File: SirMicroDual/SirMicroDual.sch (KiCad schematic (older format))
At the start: 38 parts, among them J1 Conn_01x16, J2 Conn_01x16, J3 USB_B_Micro, Q1 Q_DUAL_PMOS_S1G1D2S2G2D1, U1 ATmega32U4-MU, U2 AP2127K-3.3, U3 AP1117-50, Y1 Resonator

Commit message: Layout updated and silkscreen revised
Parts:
- removed C11: 22uF, Capacitor_Tantalum_SMD:CP_EIA-3216-18_Kemet-A_Pad1.58x1.35mm_HandSolder, symbol Device:CP
- added C?: 22uF, Capacitor_Tantalum_SMD:CP_EIA-3216-18_Kemet-A_Pad1.58x1.35mm_HandSolder, symbol Device:CP
- U2: value AP2127K-3.3 -> AP2112K-3.3
- Y1: value Resonator -> 16MHz
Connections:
- net GND: now also C?.2
- net at C2.1, Q1.1 (S), U3.3 (VI): now also C?.1
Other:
- moved on the sheet: C10, C2, C9, JP1, JP2, Q1A, R6, U2

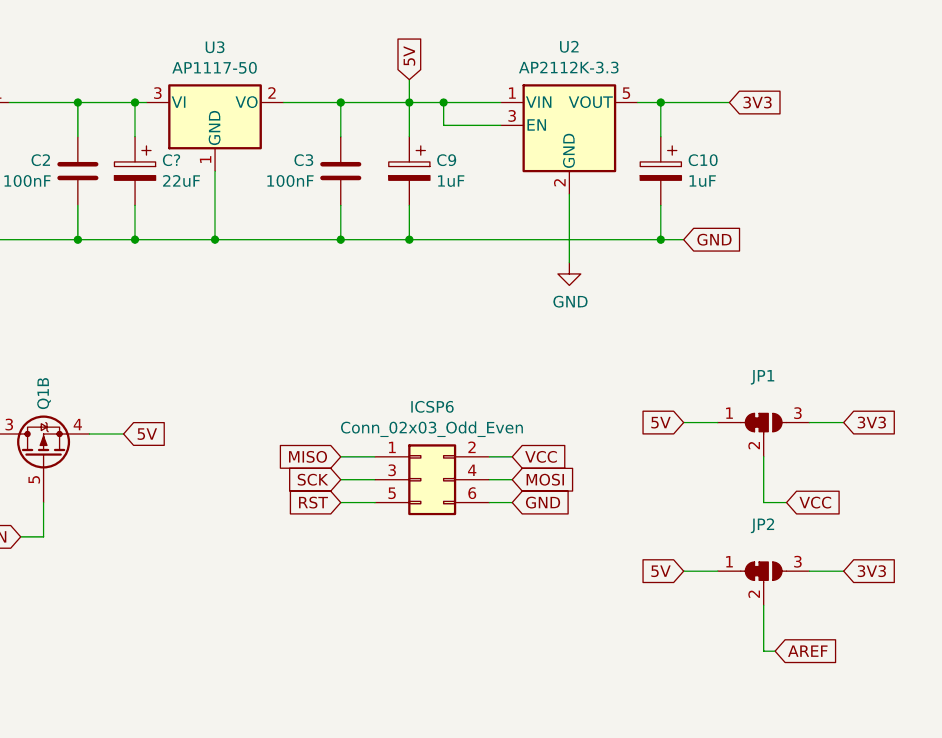
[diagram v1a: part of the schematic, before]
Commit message: LDO changed
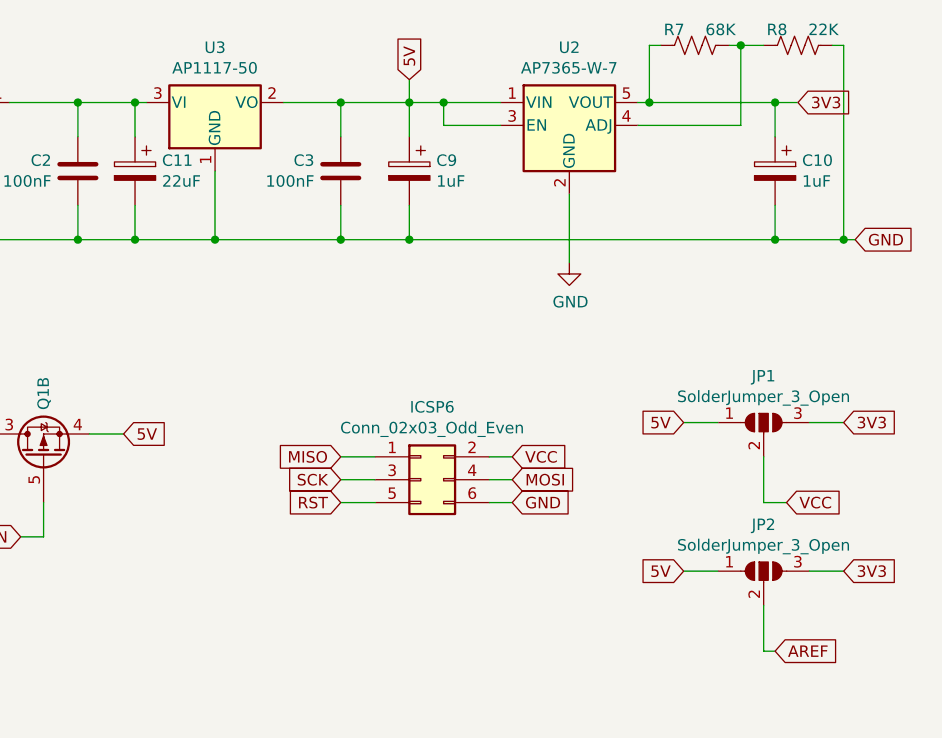
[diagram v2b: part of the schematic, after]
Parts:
- removed JP1, JP2: SolderJumper_3_Bridged12, Jumper:SolderJumper-3_P1.3mm_Bridged12_RoundedPad1.0x1.5mm, symbol Jumper:SolderJumper_3_Bridged12
- removed U2: AP2112K-3.3, Package_TO_SOT_SMD:SOT-23-5, symbol Regulator_Linear:AP2127K-3.3
- added JP1, JP2: SolderJumper_3_Open, Jumper:SolderJumper-3_P1.3mm_Open_RoundedPad1.0x1.5mm, symbol Jumper:SolderJumper_3_Open
- added R7: 68K, Resistor_SMD:R_0603_1608Metric, symbol Device:R_US
- added R8: 22K, Resistor_SMD:R_0603_1608Metric, symbol Device:R_US
- added U2: AP7365-W-7, Package_TO_SOT_SMD:SOT-23-5, symbol Regulator_Linear:AP2127K-ADJ
- F1: footprint Resistor_SMD:R_1210_3225Metric_Pad1.42x2.65mm_HandSolder -> Resistor_SMD:R_1206_3216Metric
- gave numbers to parts that had none: 1
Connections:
- net 3V3: now also JP1.3 (B), JP2.3 (B), R7.1, U2.5 (VOUT)
- net 5V: now also JP1.1 (A), JP2.1 (A), U2.1 (VIN), U2.3 (EN)
- net AREF: now also JP2.2 (C)
- net GND: now also R8.2, U2.2 (GND)
- net VCC: now also JP1.2 (C)
- new net: R7.2, R8.1, U2.4 (ADJ)
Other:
- moved on the sheet: C10
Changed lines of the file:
@@
 F 0 "F1" H 2088 2796 50  0000 L CNN
 F 1 "500mA" H 2088 2705 50  0000 L CNN
-F 2 "Resistor_SMD:R_1210_3225Metric_Pad1.42x2.65mm_HandSolder" H 2050 2550 50  0001 L CNN
+F 2 "Resistor_SMD:R_1206_3216Metric" H 2050 2550 50  0001 L CNN
 F 3 "~" H 2000 2750 50  0001 C CNN
 	1    2000 2750
@@
 L Device:CP C10
 U 1 1 5D5B70AC
-P 9900 1850
-F 0 "C10" H 9782 1896 50  0000 R CNN
-F 1 "1uF" H 9782 1805 50  0000 R CNN
-F 2 "Capacitor_SMD:C_0805_2012Metric_Pad1.15x1.40mm_HandSolder" H 9938 1700 50  0001 C CNN
-F 3 "~" H 9900 1850 50  0001 C CNN
-	1    9900 1850
+P 10400 1850
+F 0 "C10" H 10282 1896 50  0000 R CNN
+F 1 "1uF" H 10282 1805 50  0000 R CNN
+F 2 "Capacitor_SMD:C_0805_2012Metric_Pad1.15x1.40mm_HandSolder" H 10438 1700 50  0001 C CNN
+F 3 "~" H 10400 1850 50  0001 C CNN
+	1    10400 1850
 	-1   0    0    -1
 $EndComp
 Wire Wire Line
-	9900 1700 9900 1550
+	10400 1700 10400 1550
 $Comp
 L Device:CP C9
@@
 Text GLabel 2000 2350 0    50   Input ~ 0
 VUSB
-Text GLabel 10200 1550 2    50   Input ~ 0
+Text GLabel 10500 1550 2    50   Input ~ 0
 3V3
 Text GLabel 5150 4850 2    50   Input ~ 0
@@
 5V
 Wire Wire Line
-	10200 1550 9900 1550
-Connection ~ 9900 1550
+	10500 1550 10400 1550
+Connection ~ 10400 1550
 Text GLabel 9400 4800 0    50   Input ~ 0
 3V3
@@
 Text GLabel 2400 1450 0    50   Input ~ 0
 VCC
-$Comp
-L Jumper:SolderJumper_3_Bridged12 JP1
-U 1 1 5D43EA60
-P 10350 2950
-F 0 "JP1" H 10350 3153 50  0000 C CNN
-F 1 "SolderJumper_3_Bridged12" H 10350 3063 50  0001 C CNN
-F 2 "Jumper:SolderJumper-3_P1.3mm_Bridged12_RoundedPad1.0x1.5mm" H 10350 2950 50  0001 C CNN
-F 3 "~" H 10350 2950 50  0001 C CNN
-	1    10350 2950
-	1    0    0    -1
-$EndComp
 Text GLabel 10000 2950 0    50   Input ~ 0
 5V
@@
 Wire Wire Line
 	10150 2950 10000 2950
-$Comp
-L Jumper:SolderJumper_3_Bridged12 JP2
-U 1 1 5D523778
-P 10350 3600
-F 0 "JP2" H 10350 3803 50  0000 C CNN
-F 1 "SolderJumper_3_Bridged12" H 10350 3713 50  0001 C CNN
-F 2 "Jumper:SolderJumper-3_P1.3mm_Bridged12_RoundedPad1.0x1.5mm" H 10350 3600 50  0001 C CNN
-F 3 "~" H 10350 3600 50  0001 C CNN
-	1    10350 3600
-	1    0    0    -1
-$EndComp
 Wire Wire Line
 	4500 2150 4500 1700
@@
 	4300 1850 4300 2150
 Wire Wire Line
-	9800 1550 9900 1550
-Wire Wire Line
 	9200 1650 8950 1650
 Wire Wire Line
 	8950 1550 9200 1550
-$Comp
-L Regulator_Linear:AP2127K-3.3 U2
-U 1 1 5D591962
-P 9500 1650
-F 0 "U2" H 9500 1992 50  0000 C CNN
-F 1 "AP2112K-3.3" H 9500 1901 50  0000 C CNN
-F 2 "Package_TO_SOT_SMD:SOT-23-5" H 9500 1975 50  0001 C CNN
-F 3 "https://www.diodes.com/assets/Datasheets/AP2127.pdf" H 9500 1750 50  0001 C CNN
-	1    9500 1650
-	1    0    0    -1
-$EndComp
-Wire Wire Line
-	8800 2150 9900 2150
-Wire Wire Line
-	9900 2000 9900 2150
+Wire Wire Line
+	8800 2150 10400 2150
+Wire Wire Line
+	10400 2000 10400 2150
 Wire Wire Line
 	8800 2000 8800 2150
@@
 Wire Wire Line
 	5900 5950 5800 5950
-Text GLabel 10000 2150 2    50   Input ~ 0
+Text GLabel 10750 2150 2    50   Input ~ 0
 GND
 Wire Wire Line
-	10000 2150 9900 2150
+	10750 2150 10700 2150
 Wire Wire Line
 	7350 1700 7350 1550
@@
 $EndComp
 $Comp
-L Device:CP C?
+L Device:CP C11
 U 1 1 5D5B301A
 P 7600 1850
-F 0 "C?" H 7482 1896 50  0000 R CNN
+F 0 "C11" H 7482 1896 50  0000 R CNN
 F 1 "22uF" H 7482 1805 50  0000 R CNN
 F 2 "Capacitor_Tantalum_SMD:CP_EIA-3216-18_Kemet-A_Pad1.58x1.35mm_HandSolder" H 7638 1700 50  0001 C CNN
@@
 Wire Wire Line
 	8500 1550 8800 1550
-Connection ~ 9900 2150
+Connection ~ 10400 2150
 Connection ~ 8500 1550
 Connection ~ 8500 2150
@@
 	2400 1450 2550 1450
 Connection ~ 2550 1450
+$Comp
+L Jumper:SolderJumper_3_Open JP1
+U 1 1 5E257EEF
+P 10350 2950
+F 0 "JP1" H 10350 3153 50  0000 C CNN
+F 1 "SolderJumper_3_Open" H 10350 3063 50  0000 C CNN
+F 2 "Jumper:SolderJumper-3_P1.3mm_Open_RoundedPad1.0x1.5mm" H 10350 2950 50  0001 C CNN
+F 3 "~" H 10350 2950 50  0001 C CNN
+	1    10350 2950
+	1    0    0    -1
+$EndComp
+$Comp
+L Jumper:SolderJumper_3_Open JP2
+U 1 1 5E258F47
+P 10350 3600
+F 0 "JP2" H 10350 3803 50  0000 C CNN
+F 1 "SolderJumper_3_Open" H 10350 3713 50  0000 C CNN
+F 2 "Jumper:SolderJumper-3_P1.3mm_Open_RoundedPad1.0x1.5mm" H 10350 3600 50  0001 C CNN
+F 3 "~" H 10350 3600 50  0001 C CNN
+	1    10350 3600
+	1    0    0    -1
+$EndComp
+$Comp
+L Regulator_Linear:AP2127K-ADJ U2
+U 1 1 5E2BA0AD
+P 9500 1650
+F 0 "U2" H 9500 1990 50  0000 C CNN
+F 1 "AP7365-W-7" H 9500 1900 50  0000 C CNN
+F 2 "Package_TO_SOT_SMD:SOT-23-5" H 9500 1975 50  0001 C CNN
+F 3 "https://www.diodes.com/assets/Datasheets/AP2127.pdf" H 9500 1750 50  0001 C CNN
+	1    9500 1650
+	1    0    0    -1
+$EndComp
+$Comp
+L Device:R_US R7
+U 1 1 5E34715F
+P 10050 1300
+F 0 "R7" V 10118 1346 50  0000 L CNN
+F 1 "68K" V 10118 1255 50  0000 R CNN
+F 2 "Resistor_SMD:R_0603_1608Metric" V 10090 1290 50  0001 C CNN
+F 3 "~" H 10050 1300 50  0001 C CNN
+	1    10050 1300
+	0    -1   -1   0
+$EndComp
+$Comp
+L Device:R_US R8
+U 1 1 5E35753D
+P 10500 1300
+F 0 "R8" V 10568 1346 50  0000 L CNN
+F 1 "22K" V 10568 1255 50  0000 R CNN
+F 2 "Resistor_SMD:R_0603_1608Metric" V 10540 1290 50  0001 C CNN
+F 3 "~" H 10500 1300 50  0001 C CNN
+	1    10500 1300
+	0    -1   -1   0
+$EndComp
+Wire Wire Line
+	10250 1650 9800 1650
+Wire Wire Line
+	10200 1300 10250 1300
+Wire Wire Line
+	10650 1300 10700 1300
+Wire Wire Line
+	10700 1300 10700 2150
+Connection ~ 10700 2150
+Wire Wire Line
+	10700 2150 10400 2150
+Wire Wire Line
+	9800 1550 9850 1550
+Wire Wire Line
+	10250 1650 10250 1300
+Connection ~ 10250 1300
+Wire Wire Line
+	10250 1300 10350 1300
+Wire Wire Line
+	9900 1300 9850 1300
+Wire Wire Line
+	9850 1300 9850 1550
+Connection ~ 9850 1550
+Wire Wire Line
+	9850 1550 10400 1550
 $EndSCHEMATC

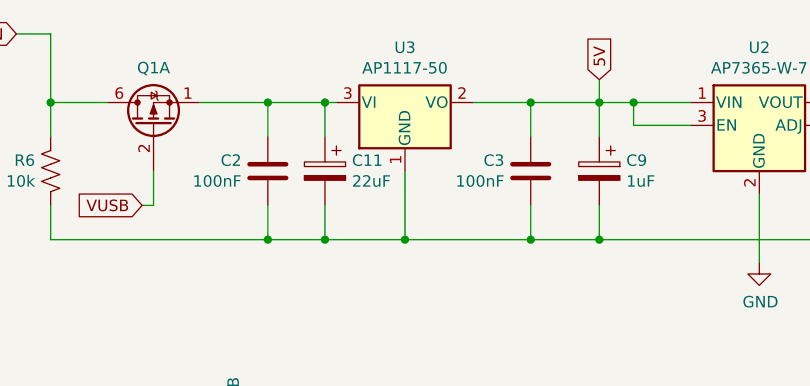
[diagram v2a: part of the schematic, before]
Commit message: Regulator changed from AP to AZ
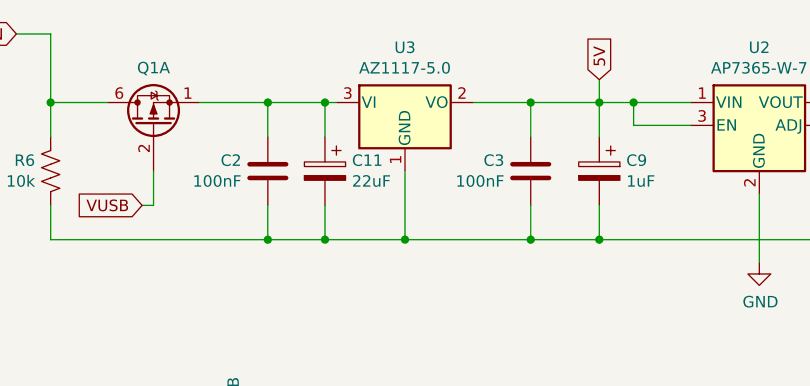
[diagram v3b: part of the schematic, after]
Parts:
- removed U3: AP1117-50, Package_TO_SOT_SMD:SOT-223-3_TabPin2, symbol Regulator_Linear:AP1117-50
- added U3: AZ1117-5.0, Package_TO_SOT_SMD:SOT-223-3_TabPin2, symbol Regulator_Linear:AZ1117-5.0
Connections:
- net 5V: now also U3.2 (VO)
- net GND: now also U3.1 (GND)
- net at C11.1, C2.1, Q1.1 (S): now also U3.3 (VI)
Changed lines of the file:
@@
 Wire Wire Line
 	8800 2000 8800 2150
-$Comp
-L Regulator_Linear:AP1117-50 U3
-U 1 1 5D488AB8
-P 7950 1550
-F 0 "U3" H 7950 1790 50  0000 C CNN
-F 1 "AP1117-50" H 7950 1700 50  0000 C CNN
-F 2 "Package_TO_SOT_SMD:SOT-223-3_TabPin2" H 7950 1750 50  0001 C CNN
-F 3 "http://www.diodes.com/datasheets/AP1117.pdf" H 8050 1300 50  0001 C CNN
-	1    7950 1550
-	1    0    0    -1
-$EndComp
 Wire Wire Line
 	8250 1550 8500 1550
@@
 Wire Wire Line
 	9850 1550 10400 1550
+$Comp
+L Regulator_Linear:AZ1117-5.0 U3
+U 1 1 5D85B6BD
+P 7950 1550
+F 0 "U3" H 7950 1790 50  0000 C CNN
+F 1 "AZ1117-5.0" H 7950 1700 50  0000 C CNN
+F 2 "Package_TO_SOT_SMD:SOT-223-3_TabPin2" H 7950 1800 50  0001 C CIN
+F 3 "https://www.diodes.com/assets/Datasheets/AZ1117.pdf" H 7950 1550 50  0001 C CNN
+	1    7950 1550
+	1    0    0    -1
+$EndComp
 $EndSCHEMATC

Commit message: Capacitor Footprint change
3216 to 3512
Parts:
- C11: footprint Capacitor_Tantalum_SMD:CP_EIA-3216-18_Kemet-A_Pad1.58x1.35mm_HandSolder -> Capacitor_Tantalum_SMD:CP_EIA-3528-12_Kemet-T
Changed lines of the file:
@@
 F 0 "C11" H 7482 1896 50  0000 R CNN
 F 1 "22uF" H 7482 1805 50  0000 R CNN
-F 2 "Capacitor_Tantalum_SMD:CP_EIA-3216-18_Kemet-A_Pad1.58x1.35mm_HandSolder" H 7638 1700 50  0001 C CNN
+F 2 "Capacitor_Tantalum_SMD:CP_EIA-3528-12_Kemet-T" H 7638 1700 50  0001 C CNN
 F 3 "~" H 7600 1850 50  0001 C CNN
 	1    7600 1850
